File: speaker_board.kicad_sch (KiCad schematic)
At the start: 3 parts, among them J2 MP3_Module

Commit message: UPDATED schematic
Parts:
- removed J2: MP3_Module, Connector_PinSocket_2.54mm:PinSocket_2x08_P2.54mm_Vertical, symbol Connector_Generic:Conn_02x08_Counter_Clockwise
- added J1: MP3_Module_Left, Connector_PinSocket_2.54mm:PinSocket_1x08_P2.54mm_Vertical, symbol Connector:Conn_01x08_Socket
- added J2: Conn_01x14_Female, rsx_headers:PinSocket_1x14_P2.54mm_Vertical, symbol rsx_header:Conn_01x14_Female
- added J3: MP3_Module_Right, Connector_PinSocket_2.54mm:PinSocket_1x08_P2.54mm_Vertical, symbol Connector:Conn_01x08_Socket
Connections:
- net +5V: now also J1.1 (VCC)
- net GND: now also J1.7 (GND)
- net MP3_RX: now reaches A1.17 (D2)
- net MP3_RX: now also J1.2 (Pin_2)
- net MP3_TX: now reaches A1.18 (D3)
- net MP3_TX: now also J1.3 (TX)
- net SPK_1: now reaches LS1.1
- net SPK_1: now also J1.6 (SPK_1)
- net SPK_2: now reaches LS1.2
- net SPK_2: now also J1.8 (SPK_2)
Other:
- moved on the sheet: LS1

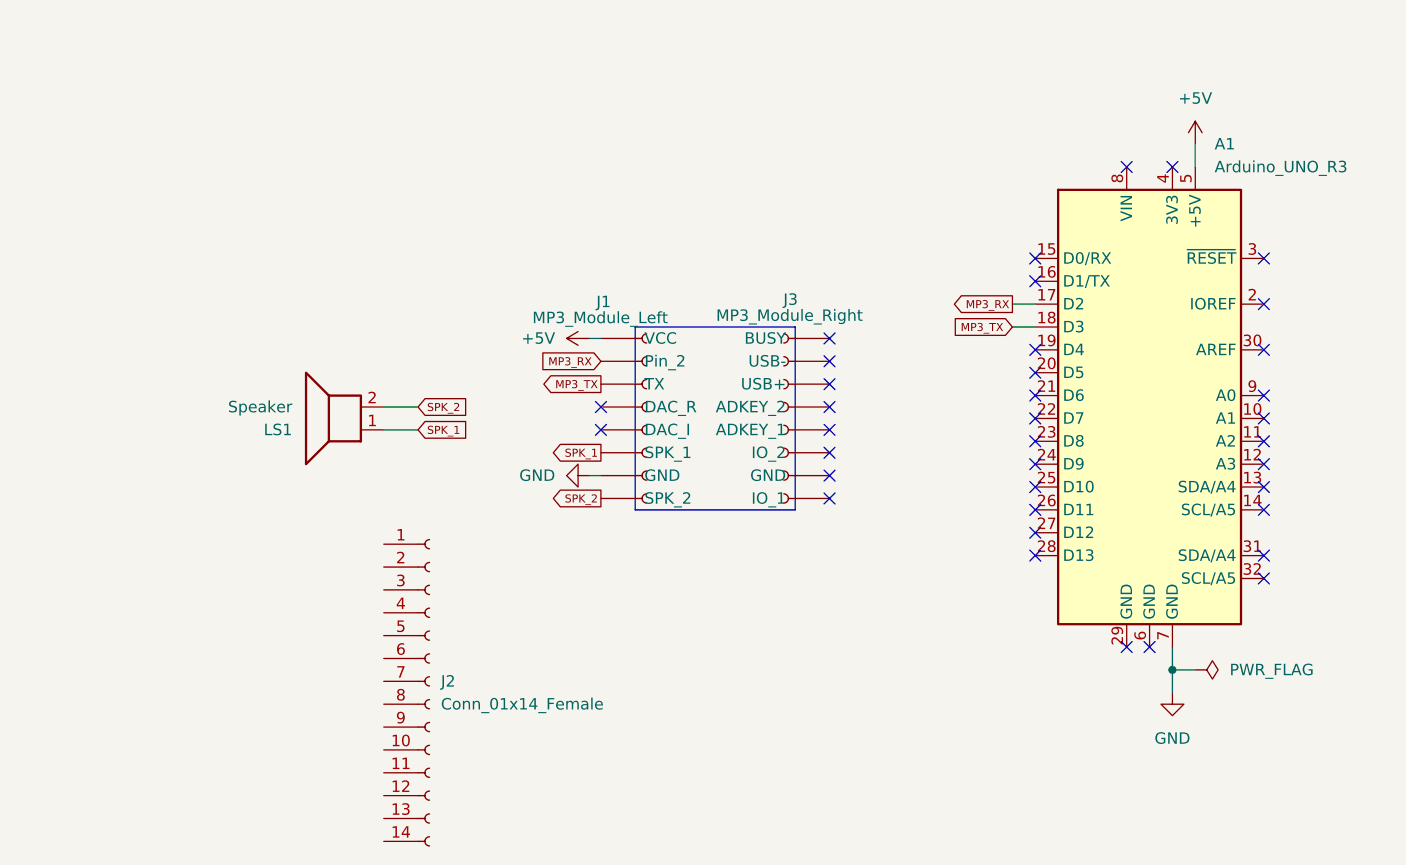
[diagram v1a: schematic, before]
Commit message: Board with updated components
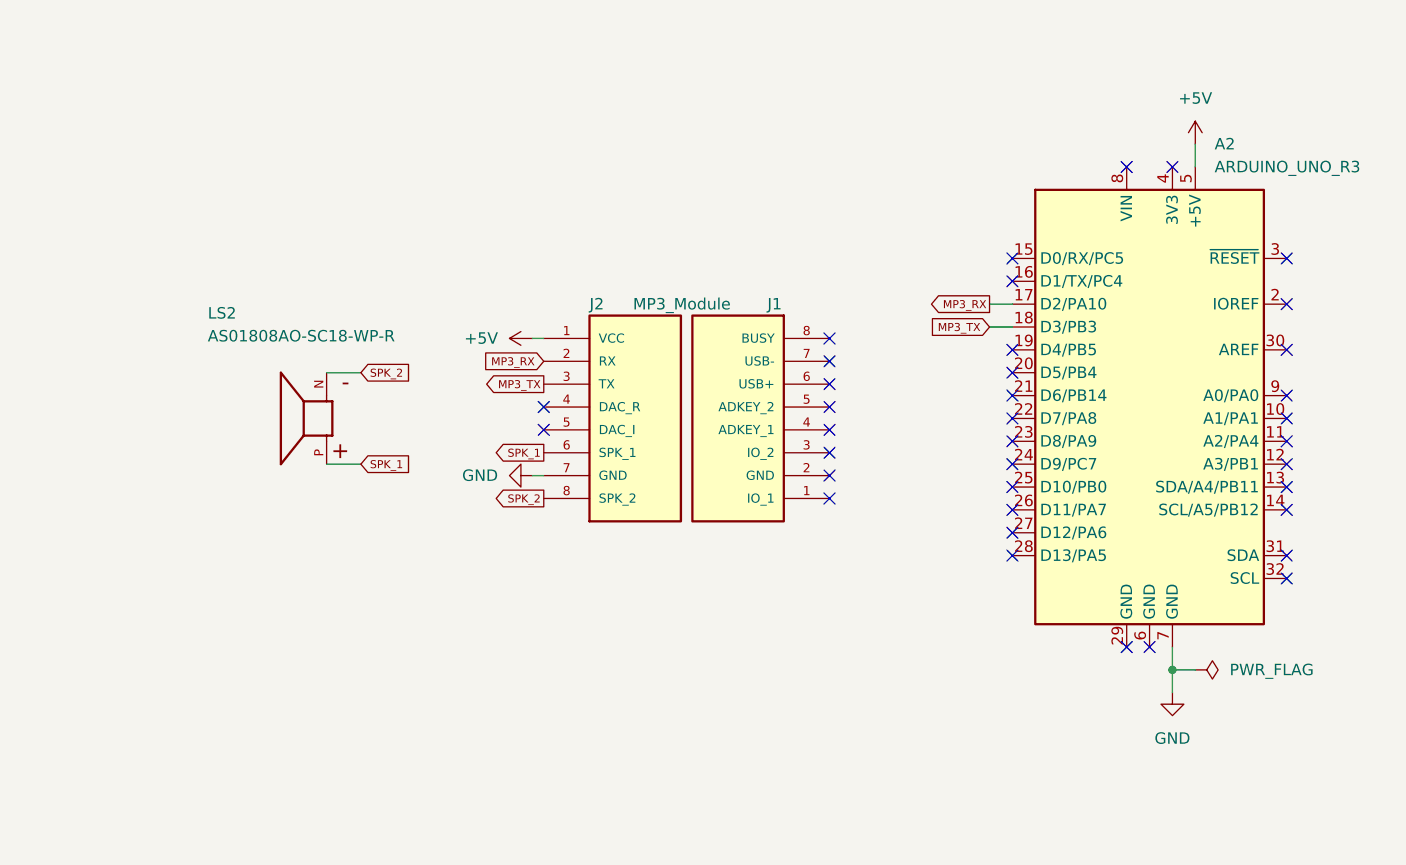
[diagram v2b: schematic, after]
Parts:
- removed A1: Arduino_UNO_R3, Module:Arduino_UNO_R3, symbol MCU_Module:Arduino_UNO_R3
- removed J1: MP3_Module_Left, Connector_PinSocket_2.54mm:PinSocket_1x08_P2.54mm_Vertical, symbol Connector:Conn_01x08_Socket
- removed J2: Conn_01x14_Female, rsx_headers:PinSocket_1x14_P2.54mm_Vertical, symbol rsx_header:Conn_01x14_Female
- removed J3: MP3_Module_Right, Connector_PinSocket_2.54mm:PinSocket_1x08_P2.54mm_Vertical, symbol Connector:Conn_01x08_Socket
- removed LS1: Speaker, Connector_PinHeader_2.54mm:PinHeader_1x02_P2.54mm_Vertical, symbol Device:Speaker
- added A2: ARDUINO_UNO_R3, rsx_modules:STM32_NUCLEO64_ArduinoUno, symbol rsx_Modules:ARDUINO_UNO_R3
- added J1: SSK02-FPH-254-A8, rsx_misc:SAMESKY_SSK02-FPH-254-A8, symbol rsx_misc:SSK02-FPH-254-A8
- added J2: MP3_Module, rsx_misc:SAMESKY_SSK02-FPH-254-A8, symbol rsx_misc:SSK02-FPH-254-A8
- added LS2: AS01808AO-SC18-WP-R, rsx_sensors:SPKR_AS01808AO-SC18-WP-R, symbol rsx_sensors:AS01808AO-SC18-WP-R
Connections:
- net +5V: now also A2.5 (+5V), J2.1 (VCC)
- net GND: now also A2.7 (GND), J2.7 (GND)
- net MP3_RX: now also A2.17 (D2/PA10), J2.2 (RX)
- net MP3_TX: now also A2.18 (D3/PB3), J2.3 (TX)
- net SPK_1: now also J2.6 (SPK_1), LS2.P
- net SPK_2: now also J2.8 (SPK_2), LS2.N
